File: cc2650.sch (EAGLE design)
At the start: 23 parts, among them IC4 CC2650MODAMOHR, SW1 SPST_TACT-KMR2, SW2 SPST_TACT-KMR2, U402 TPS62237DRY

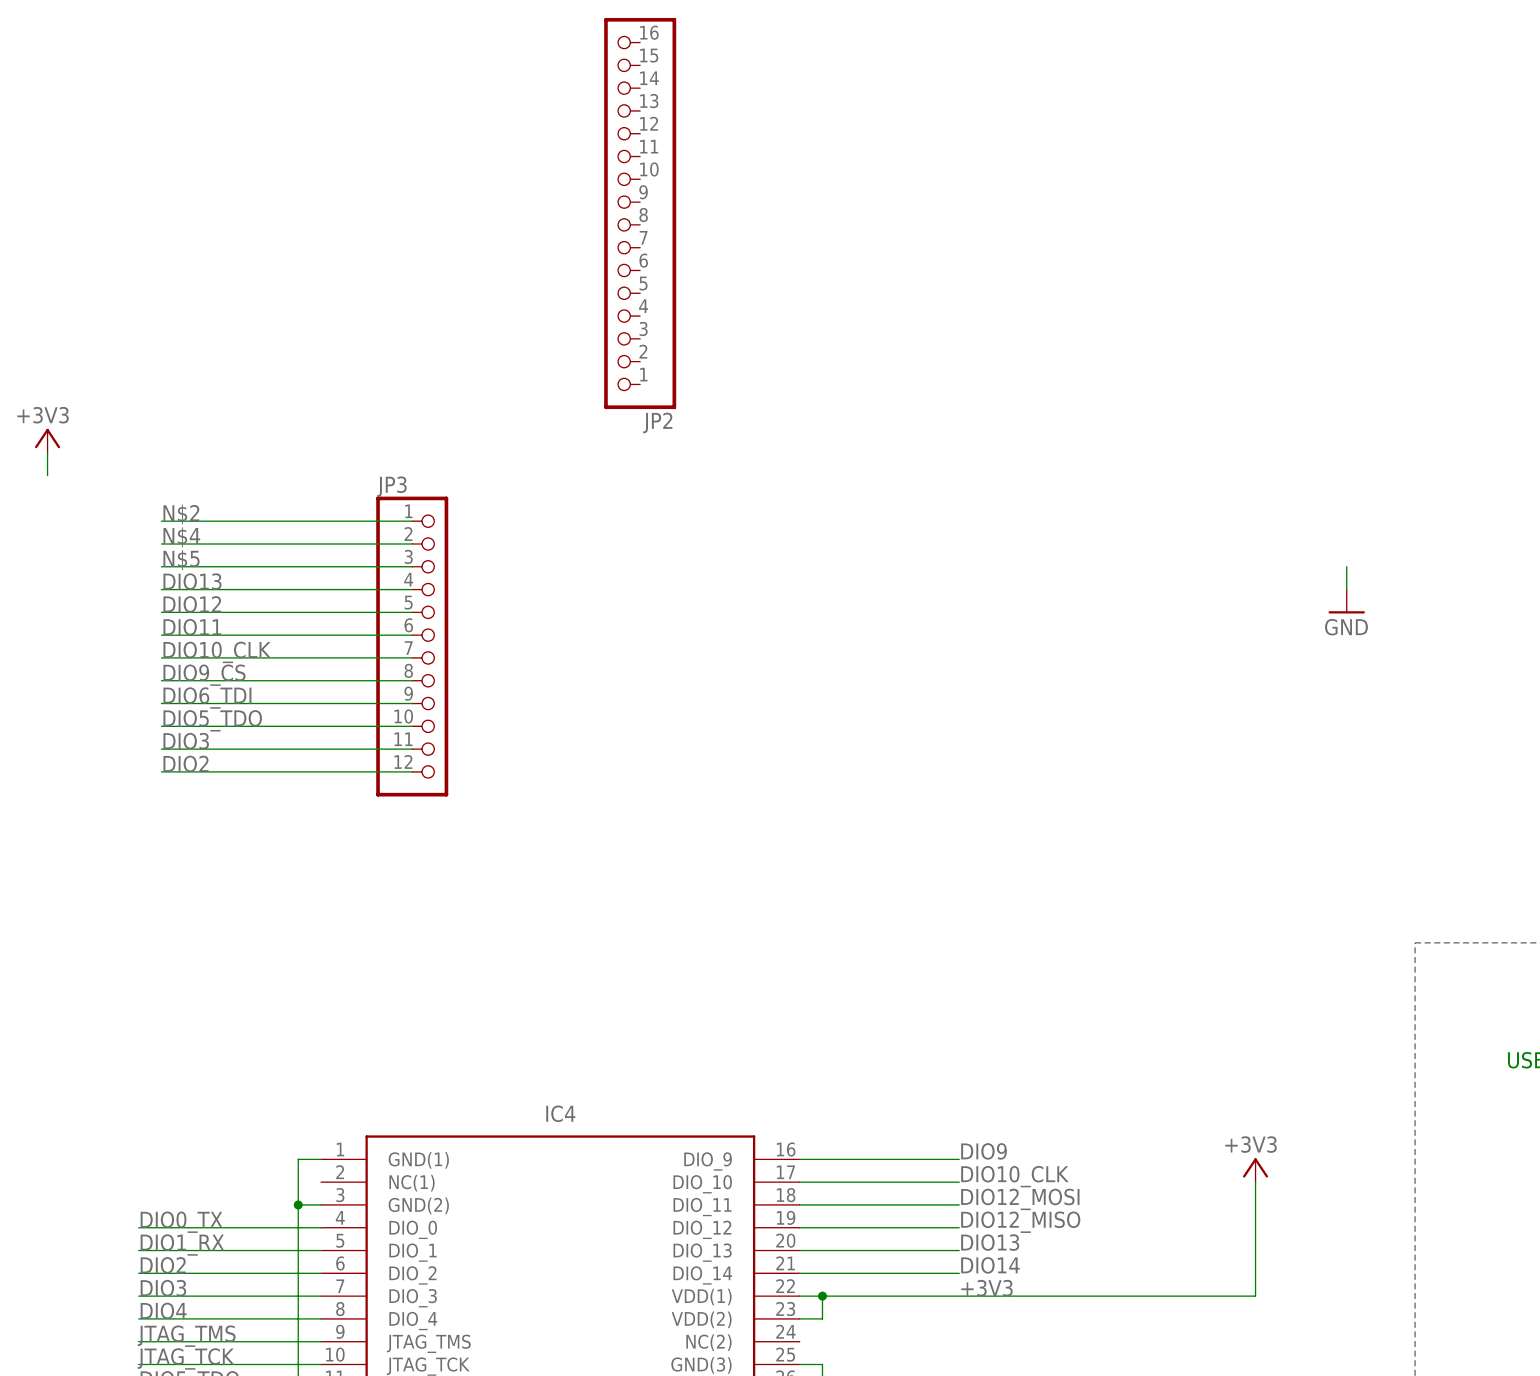
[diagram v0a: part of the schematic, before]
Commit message: changed pinout.
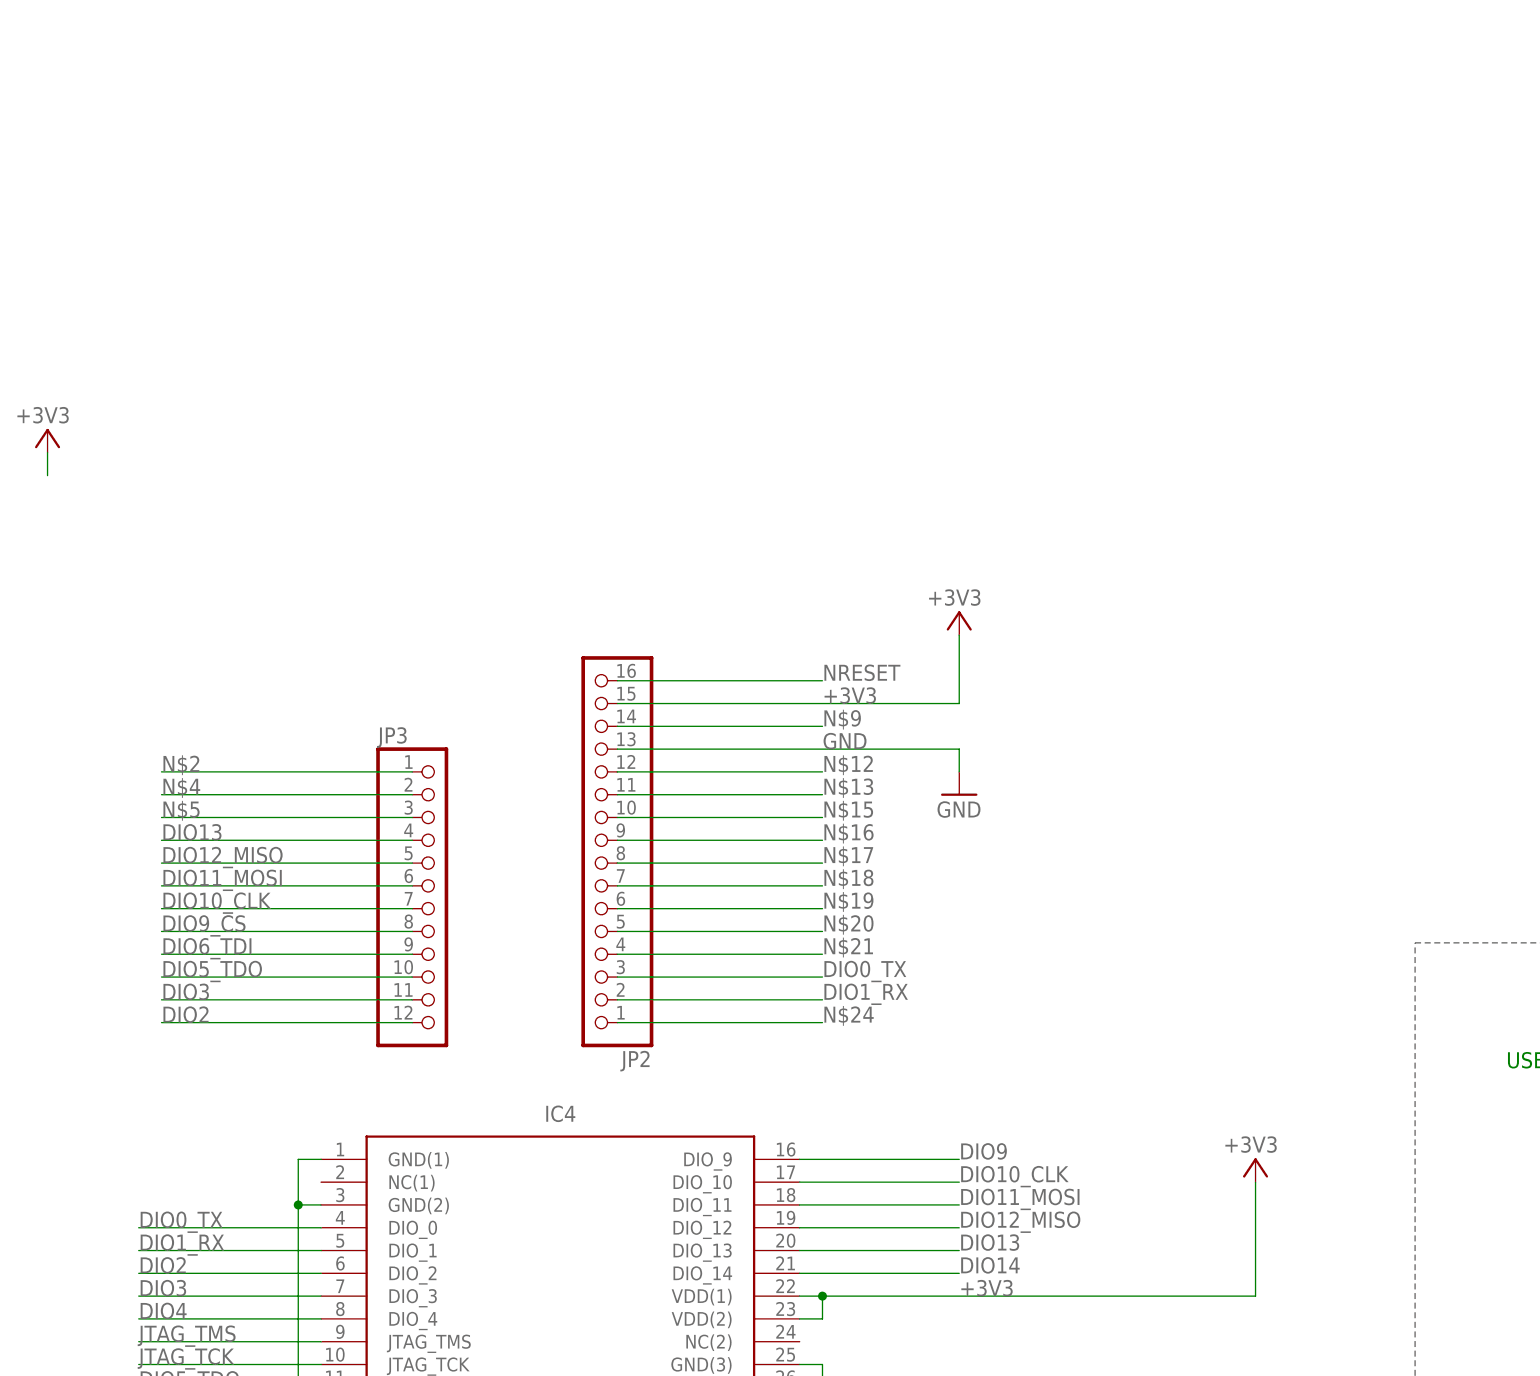
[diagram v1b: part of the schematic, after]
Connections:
- removed net DIO11: JP3.6
- removed net DIO12: JP3.5
- removed net DIO12_MOSI: IC4.DIO_11
- new net DIO11_MOSI: IC4.DIO_11, JP3.6
- new net N$12: JP2.12
- new net N$13: JP2.11
- new net N$15: JP2.10
- new net N$16: JP2.9
- new net N$17: JP2.8
- new net N$18: JP2.7
- new net N$19: JP2.6
- new net N$20: JP2.5
- new net N$21: JP2.4
- new net N$24: JP2.1
- new net N$9: JP2.14
- net +3V3: now also JP2.15
- net DIO0_TX: now also JP2.3
- net DIO12_MISO: now also JP3.5
- net DIO1_RX: now also JP2.2
- net GND: now also JP2.13
- net NRESET: now also JP2.16
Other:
- moved on the sheet: JP2, JP3
